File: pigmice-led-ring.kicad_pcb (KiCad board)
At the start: 2 copper layers, 46 x 51 mm, 58 parts, among them J1 Conn_01x02_Female, J2 Conn_01x03_Female, SW1 SW_Push, U1 LMR62014XMF

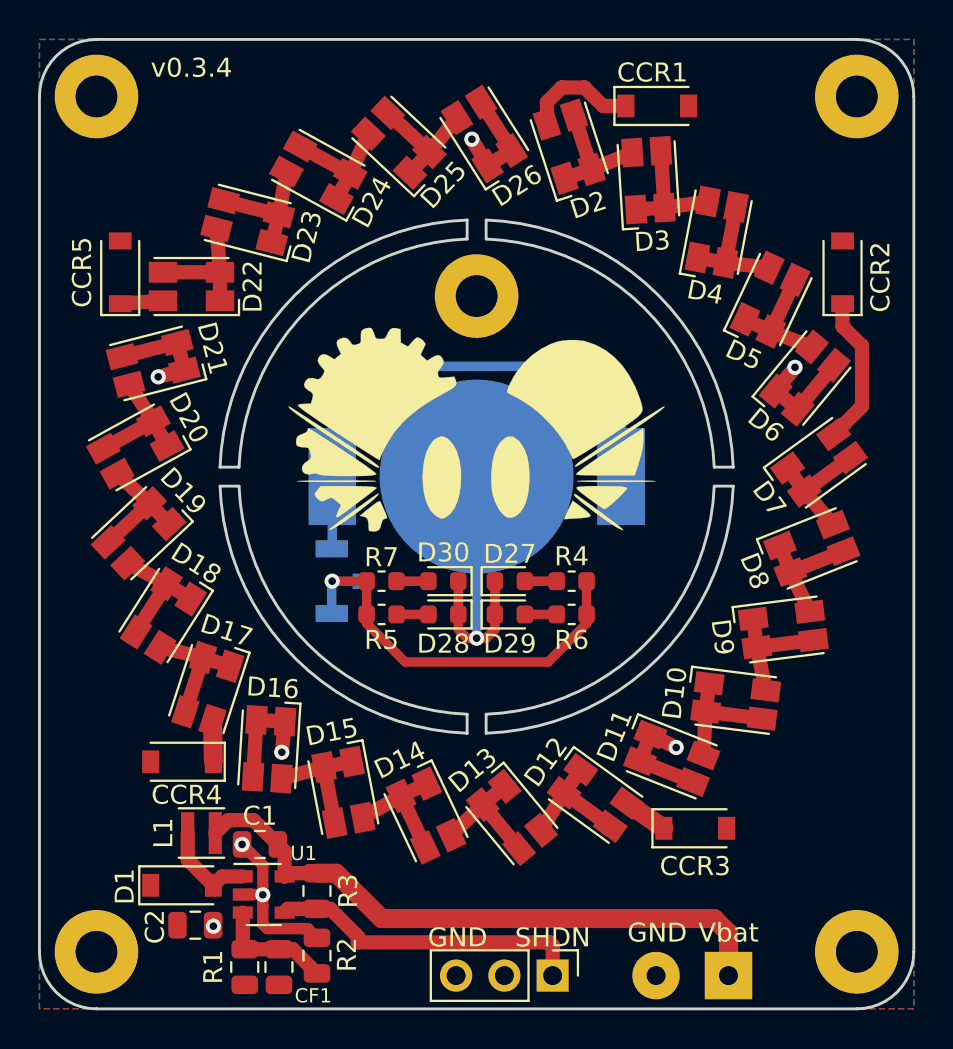
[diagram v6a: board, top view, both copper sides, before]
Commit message: Powerpole, DFM, optimize BOM
* Optimizes BOM to use cheaper components (~$15 components per board)
* Change power connector to use an Anderson connector
* Some DFM (remove copper fill logo, center part)
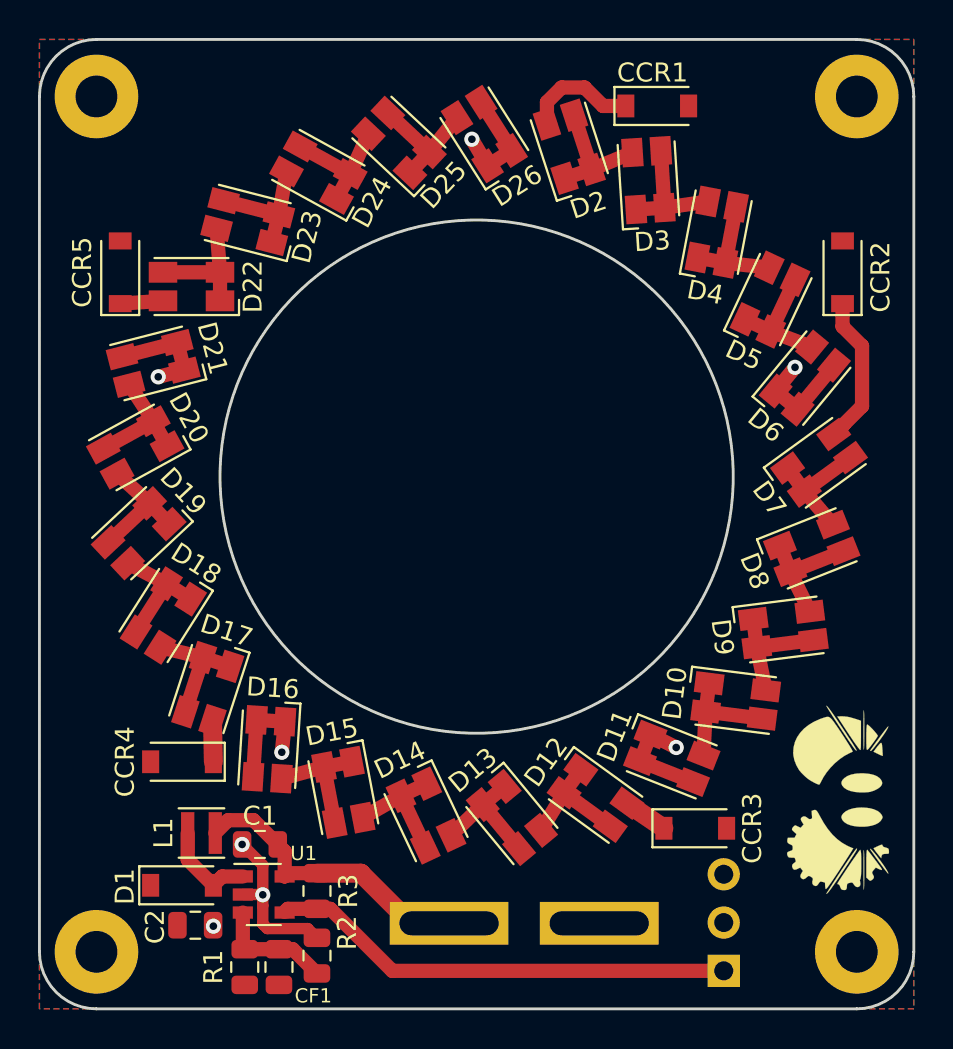
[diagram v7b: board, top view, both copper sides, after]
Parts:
- removed BT1: Battery_Cell, Battery:BatteryHolder_LINX_BAT-HLD-012-SMT
- removed D27, D28, D29, D30: LED, LED_SMD:LED_0603_1608Metric
- removed the G*** at (90.0, 77.5)
- removed R4, R5: 47Ω, Resistor_SMD:R_0603_1608Metric
- removed R6, R7: 56Ω, Resistor_SMD:R_0603_1608Metric
- removed the REF** at (90.0, 70.5)
- removed SW1: SW_Push, Button_Switch_SMD:SW_SPST_B3U-1100P
- added REF**: OSHW-Symbol_6.7x6mm_SilkScreen, Symbol:OSHW-Symbol_6.7x6mm_SilkScreen, B.Cu at (76.5, 60.5)
- J1: footprint Connector_Wire:SolderWirePad_1x02_P3.81mm_Drill1mm -> Connectors_Anderson:45A-VERT-PAIR; moved to B.Cu
- J2: moved to B.Cu
- moved J1 11.1 mm to (92.5, 103.5), turned to 0 degrees
- moved J2 9.00 mm to (103.0, 106.0), turned to 0 degrees
- moved G*** 0.71 mm to (109.0, 97.0)
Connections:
- J2 pad 2: (no net) -> Net-(J2-Pad2)
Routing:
- net Net-(BT1-Pad1): track 27.4 -> 0.00 mm
- net Net-(R4-Pad1): track 21.2 -> 0.00 mm, vias 1 -> 0
- net /Vbat: track 33.1 -> 16.0 mm
- net Net-(BT1-Pad2): track 15.9 -> 0.00 mm, vias 1 -> 0
- net /SHDN: track 17.0 -> 24.8 mm
- net Net-(D30-Pad2): track 1.68 -> 0.00 mm
- net Net-(D29-Pad2): track 1.68 -> 0.00 mm
- net Net-(D28-Pad2): track 1.68 -> 0.00 mm
- net Net-(D27-Pad2): track 1.68 -> 0.00 mm
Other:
- outline, holes or cut-outs redrawn
- board text added: "github.com/Pigmice2733/led-ring v0.3.5"
- board text removed: "v0.3.4"

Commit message: Move over powerpole/PWM connector a bit
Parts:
- moved J2 1.50 mm to (101.5, 106.0)
- moved J1 1.00 mm to (91.5, 103.5)
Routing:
- net /SHDN: track 24.8 -> 23.8 mm
- net /Vbat: track 16.0 -> 17.0 mm
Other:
- board text added: "github.com/Pigmice2733/led-ring v0.3.6"
- board text removed: "github.com/Pigmice2733/led-ring v0.3.5"
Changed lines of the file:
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@@
     (thickness 1.6)
     (drawings 14)
-    (tracks 133)
+    (tracks 136)
     (zones 0)
     (modules 47)
@@
   )
   (module Connector_PinHeader_2.54mm:PinHeader_1x03_P2.54mm_Vertical (layer B.Cu)
-    (at 103 106)
+    (at 101.5 106)
     (descr "Through hole straight pin header, 1x03, 2.54mm pitch, single row")
     (tags "Through hole pin header THT 1x03 2.54mm single row")
@@
   )
   (module Connectors_Anderson:45A-VERT-PAIR (layer B.Cu)
-    (at 92.5 103.5)
+    (at 91.5 103.5)
     (descr "Use through-hole center to align with adjacent PowerPole connectors.  Do not rely on housing outlines.")
     (tags "Anderson Powerpole 25A PCB right angle G2")
@@
     )
   )
-  (gr_text "github.com/Pigmice2733/led-ring\nv0.3.5" (at 107 60) (layer B.SilkS)
+  (gr_text "github.com/Pigmice2733/led-ring\nv0.3.6" (at 107 60) (layer B.SilkS)
     (effects (font (size 1 1) (thickness 0.15)) (justify left mirror))
   )
@@
   (gr_line (start 110 57) (end 70 57) (layer Edge.Cuts) (width 0.15))
   (gr_line (start 70 108) (end 110 108) (layer Edge.Cuts) (width 0.15))
-  (gr_text SHDN (at 105.5 105.75 90) (layer B.SilkS)
+  (gr_text SHDN (at 104 105.75 90) (layer B.SilkS)
     (effects (font (size 1 1) (thickness 0.15)) (justify mirror))
   )
-  (gr_text GND (at 105.5 101 90) (layer B.SilkS)
+  (gr_text GND (at 104 101 90) (layer B.SilkS)
     (effects (font (size 1 1) (thickness 0.15)) (justify mirror))
   )
-  (gr_text GND (at 96.5 98) (layer B.SilkS)
+  (gr_text GND (at 95.5 98) (layer B.SilkS)
     (effects (font (size 1 1) (thickness 0.15)) (justify mirror))
   )
-  (gr_text Vbat (at 88.75 98) (layer B.SilkS)
+  (gr_text Vbat (at 87.75 98) (layer B.SilkS)
     (effects (font (size 1 1) (thickness 0.15)) (justify mirror))
   )
@@
   (segment (start 78.26249 98.07499) (end 76.92501 98.07499) (width 0.75) (layer F.Cu) (net 6))
   (segment (start 86.55 103.5) (end 88.55 103.5) (width 1) (layer F.Cu) (net 6))
-  (segment (start 81.6 100.8625) (end 83.9125 100.8625) (width 1) (layer F.Cu) (net 6))
-  (segment (start 83.9125 100.8625) (end 86.55 103.5) (width 1) (layer F.Cu) (net 6))
+  (segment (start 84.9125 100.8625) (end 81.6 100.8625) (width 1) (layer F.Cu) (net 6))
+  (segment (start 87.55 103.5) (end 84.9125 100.8625) (width 1) (layer F.Cu) (net 6))
   (segment (start 99.692743 62.857561) (end 99.881114 65.851641) (width 0.75) (layer F.Cu) (net 7) (status 30))
   (segment (start 98.384075 65.945827) (end 99.881114 65.851641) (width 0.75) (layer F.Cu) (net 7) (status 30))
@@
   (segment (start 80.064463 102.7375) (end 79.9 102.901963) (width 0.75) (layer F.Cu) (net 26) (status 30))
   (segment (start 81.6 102.7375) (end 80.064463 102.7375) (width 0.75) (layer F.Cu) (net 26) (status 30))
-  (segment (start 82.3 102.7375) (end 85.5625 106) (width 0.75) (layer F.Cu) (net 26))
+  (segment (start 82.3 102.7375) (end 83.25 103.6875) (width 0.75) (layer F.Cu) (net 26))
   (segment (start 81.6 102.7375) (end 82.3 102.7375) (width 0.75) (layer F.Cu) (net 26))
-  (segment (start 85.5625 106) (end 103 106) (width 0.75) (layer F.Cu) (net 26))
+  (segment (start 99.9 106) (end 101.5 106) (width 0.75) (layer F.Cu) (net 26))
+  (segment (start 83.25 104.485002) (end 84.764998 106) (width 0.75) (layer F.Cu) (net 26))
+  (segment (start 84.764998 106) (end 99.9 106) (width 0.75) (layer F.Cu) (net 26))
+  (segment (start 83.25 103.6875) (end 83.25 104.485002) (width 0.75) (layer F.Cu) (net 26))
   (segment (start 96.65 60.5) (end 97.85 60.5) (width 0.75) (layer F.Cu) (net 27) (status 20))
   (segment (start 95.677372 59.527372) (end 96.65 60.5) (width 0.75) (layer F.Cu) (net 27))
